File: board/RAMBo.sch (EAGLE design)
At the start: 266 parts, among them Q1 PSMN7R0-60YS, Q2 PSMN7R0-60YS, Q3 PSMN7R0-60YS, Q4 IRLML6346TRPBF, Q5 PSMN7R0-60YS, Q8 IRLML6346TRPBF, U1 ATMEGA32U2-MUR, U10 ADUM7441, U2 ATMEGA2560-16AU, U3 LM22675, U4 AD5206, U5 A4982, U6 A4982, U7 A4982, U8 A4982, U9 A4982, X1 C-GRID-02-70543, X10 C-GRID-04-70543, X11 MSTBV10, X12 SPI, X13 EXT-2, X14 C-GRID-04-70543, X15 C-GRID-04-70543, X16 32u2 EXT, X17 3x2M, X18 3x2M, X2 USB B-TH, X20 MX1, X21 C-GRID-03-70543, X22 C-GRID-03-70543, X23 C-GRID-03-70543, X24 C-GRID-03-70543, X25 C-GRID-03-70543, X26 C-GRID-03-70543, X27 C-GRID-02-70543, X28 C-GRID-02-70543, X29 C-GRID-02-70543, X3 C-GRID-02-70543, X30 C-GRID-02-70543, X31 MX2, X32 MX3, X33 MSTBA6, X34 PWM_EXT, X39 M05X2PTH, X4 C-GRID-04-70543, X40 Analog, X5 C-GRID-02-70543, X6 C-GRID-04-70543, X7 C-GRID-04-70543, X8 C-GRID-04-70543, X9 C-GRID-02-70543, Y1 16MHz KX-7, Y2 16MHz KX-7

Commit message: Fix I2C schematic labels swapped
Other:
- note added: "RAMBo 1.2g"
- note removed: "RAMBo 1.2e"
- moved on the sheet: Z1, Z2
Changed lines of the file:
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@@
 <text x="308.61" y="44.45" size="3.81" layer="97">E0</text>
 <text x="419.1" y="45.72" size="3.81" layer="97">E1</text>
-<text x="251.46" y="330.2" size="6.4516" layer="97">RAMBo 1.2e</text>
+<text x="251.46" y="330.2" size="6.4516" layer="97">RAMBo 1.2g</text>
 <text x="518.16" y="322.58" size="3.81" layer="97">Atmega 32u2 USB</text>
 <text x="723.9" y="157.48" size="3.81" layer="97">I2C Expansion</text>
@@
 <instance part="U1" gate="G$1" x="541.02" y="266.7"/>
 <instance part="X17" gate="A" x="487.68" y="312.42"/>
-<instance part="Z1" gate="G$1" x="447.04" y="264.16" smashed="yes" rot="MR270">
-<attribute name="NAME" x="443.23" y="261.62" size="1.778" layer="95" rot="MR90"/>
-<attribute name="VALUE" x="450.85" y="256.54" size="1.778" layer="96" rot="MR90"/>
-</instance>
-<instance part="Z2" gate="G$1" x="457.2" y="264.16" smashed="yes" rot="MR270">
-<attribute name="NAME" x="453.39" y="261.62" size="1.778" layer="95" rot="MR90"/>
-<attribute name="VALUE" x="459.74" y="250.952" size="1.778" layer="96" rot="MR90"/>
+<instance part="Z1" gate="G$1" x="447.04" y="264.16" smashed="yes" rot="MR90">
+<attribute name="NAME" x="450.85" y="266.7" size="1.778" layer="95" rot="MR270"/>
+<attribute name="VALUE" x="445.77" y="276.86" size="1.778" layer="96" rot="MR270"/>
+</instance>
+<instance part="Z2" gate="G$1" x="457.2" y="264.16" smashed="yes" rot="MR90">
+<attribute name="NAME" x="461.01" y="266.7" size="1.778" layer="95" rot="MR270"/>
+<attribute name="VALUE" x="454.66" y="277.368" size="1.778" layer="96" rot="MR270"/>
 </instance>
 <instance part="RN5" gate="A" x="622.3" y="231.14" rot="R180"/>
@@
 </segment>
 <segment>
-<wire x1="739.14" y1="132.08" x2="728.98" y2="132.08" width="0.1524" layer="91"/>
-<label x="728.98" y="135.255" size="1.778" layer="95"/>
-<wire x1="746.76" y1="132.08" x2="739.14" y2="132.08" width="0.1524" layer="91"/>
+<wire x1="746.76" y1="132.08" x2="728.98" y2="132.08" width="0.1524" layer="91"/>
+<label x="728.98" y="132.461" size="1.778" layer="95"/>
 <wire x1="746.76" y1="137.16" x2="746.76" y2="132.08" width="0.1524" layer="91"/>
 <pinref part="R44" gate="G$1" pin="1"/>
@@
 <segment>
 <wire x1="728.98" y1="134.62" x2="739.14" y2="134.62" width="0.1524" layer="91"/>
-<label x="728.98" y="132.715" size="1.778" layer="95"/>
+<label x="728.98" y="135.001" size="1.778" layer="95"/>
 <wire x1="739.14" y1="137.16" x2="739.14" y2="134.62" width="0.1524" layer="91"/>
 <pinref part="R45" gate="G$1" pin="1"/>
@@
 <wire x1="444.5" y1="279.4" x2="447.04" y2="279.4" width="0.1524" layer="91"/>
 <wire x1="447.04" y1="279.4" x2="464.82" y2="279.4" width="0.1524" layer="91"/>
-<wire x1="447.04" y1="259.08" x2="447.04" y2="279.4" width="0.1524" layer="91"/>
+<wire x1="447.04" y1="269.24" x2="447.04" y2="279.4" width="0.1524" layer="91"/>
 <junction x="447.04" y="279.4"/>
 <label x="449.58" y="279.4" size="1.778" layer="95"/>
@@
 <wire x1="464.82" y1="276.86" x2="457.2" y2="276.86" width="0.1524" layer="91"/>
 <wire x1="457.2" y1="276.86" x2="444.5" y2="276.86" width="0.1524" layer="91"/>
-<wire x1="457.2" y1="259.08" x2="457.2" y2="276.86" width="0.1524" layer="91"/>
+<wire x1="457.2" y1="269.24" x2="457.2" y2="276.86" width="0.1524" layer="91"/>
 <wire x1="464.82" y1="271.78" x2="464.82" y2="276.86" width="0.1524" layer="91"/>
 <junction x="457.2" y="276.86"/>
@@
 <segment>
 <wire x1="436.88" y1="254" x2="436.88" y2="266.7" width="0.1524" layer="91"/>
-<wire x1="457.2" y1="269.24" x2="457.2" y2="254" width="0.1524" layer="91"/>
+<wire x1="457.2" y1="259.08" x2="457.2" y2="254" width="0.1524" layer="91"/>
 <wire x1="447.04" y1="254" x2="449.58" y2="254" width="0.1524" layer="91"/>
 <wire x1="449.58" y1="254" x2="457.2" y2="254" width="0.1524" layer="91"/>
-<wire x1="447.04" y1="269.24" x2="447.04" y2="254" width="0.1524" layer="91"/>
+<wire x1="447.04" y1="259.08" x2="447.04" y2="254" width="0.1524" layer="91"/>
 <wire x1="439.42" y1="266.7" x2="439.42" y2="254" width="0.1524" layer="91"/>
 <wire x1="439.42" y1="254" x2="447.04" y2="254" width="0.1524" layer="91"/>

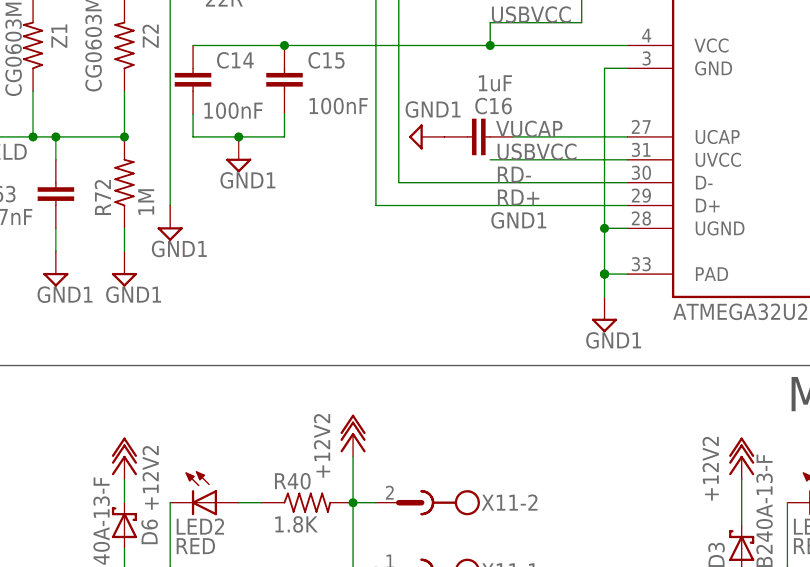
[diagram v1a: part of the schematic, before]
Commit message: add varistor for ESD protection
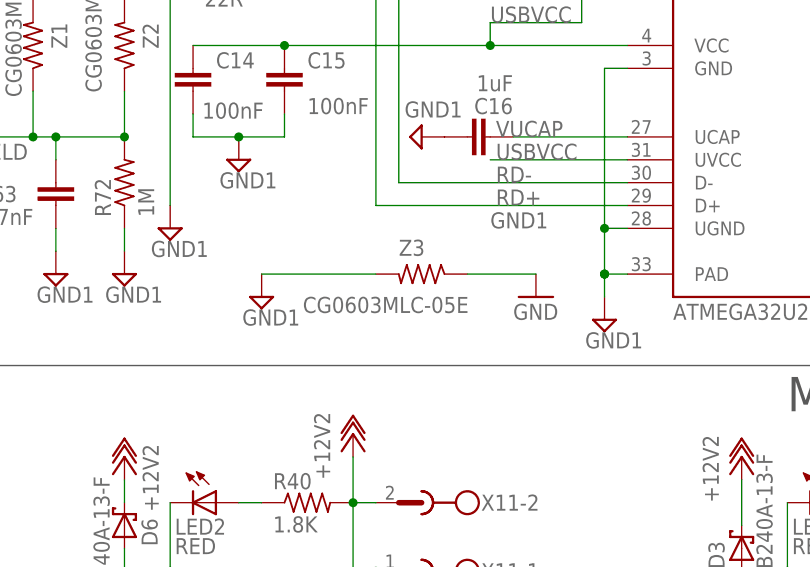
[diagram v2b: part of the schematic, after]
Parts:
- added Z3: CG0603MLC-05E, resistor:R-US_R0603
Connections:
- net GND: now also Z3.1
- net GND1: now also Z3.2
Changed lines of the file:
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@@
 <?xml version="1.0" encoding="utf-8"?>
 <!DOCTYPE eagle SYSTEM "eagle.dtd">
-<eagle version="6.4">
+<eagle version="6.5.0">
 <drawing>
 <settings>
@@
 <part name="P+46" library="ultimachine" deviceset="+12V2" device=""/>
 <part name="C63" library="rcl" deviceset="C-EU" device="C0402" value="4.7nF"/>
+<part name="Z3" library="resistor" deviceset="R-US_" device="R0603" value="CG0603MLC-05E"/>
+<part name="SUPPLY11" library="supply2" deviceset="GND1" device=""/>
+<part name="GND19" library="supply1" deviceset="GND" device=""/>
 </parts>
 <sheets>
@@
 <attribute name="VALUE" x="440.944" y="244.221" size="1.778" layer="96"/>
 </instance>
+<instance part="Z3" gate="G$1" x="490.22" y="238.76" smashed="yes" rot="MR0">
+<attribute name="NAME" x="487.68" y="242.57" size="1.778" layer="95" rot="MR180"/>
+<attribute name="VALUE" x="477.012" y="236.22" size="1.778" layer="96" rot="MR180"/>
+</instance>
+<instance part="SUPPLY11" gate="G$1" x="472.44" y="236.22"/>
+<instance part="GND19" gate="1" x="502.92" y="236.22"/>
 </instances>
 <busses>
@@
 <pinref part="GND16" gate="1" pin="GND"/>
 </segment>
+<segment>
+<pinref part="Z3" gate="G$1" pin="1"/>
+<pinref part="GND19" gate="1" pin="GND"/>
+<wire x1="502.92" y1="238.76" x2="495.3" y2="238.76" width="0.1524" layer="91"/>
+</segment>
 </net>
 <net name="VCC" class="0">
@@
 <junction x="599.44" y="307.34"/>
 </segment>
+<segment>
+<pinref part="Z3" gate="G$1" pin="2"/>
+<pinref part="SUPPLY11" gate="G$1" pin="GND1"/>
+<wire x1="485.14" y1="238.76" x2="472.44" y2="238.76" width="0.1524" layer="91"/>
+</segment>
 </net>
